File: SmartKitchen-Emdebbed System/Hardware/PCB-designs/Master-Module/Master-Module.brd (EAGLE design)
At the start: 92.3 x 59.7 mm, 24 parts, among them IC2 7805DT, J1 RJ11-2L-B, J2 RJ11-2L-B, J3 RJ11-2L-B, J4 RJ11-2L-B, Q1 BSS123, Q2 BSS123, X1 K375M

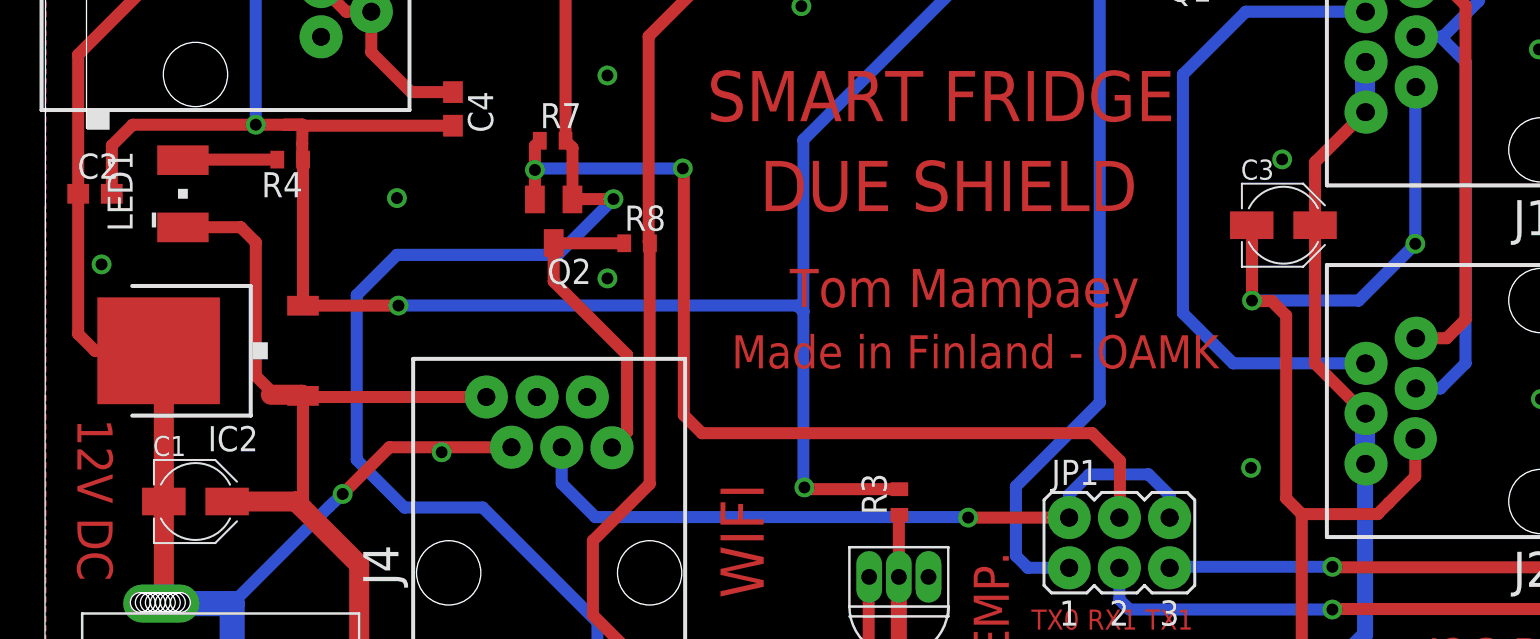
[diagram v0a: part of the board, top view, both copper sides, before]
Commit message: Redesigned wrong component
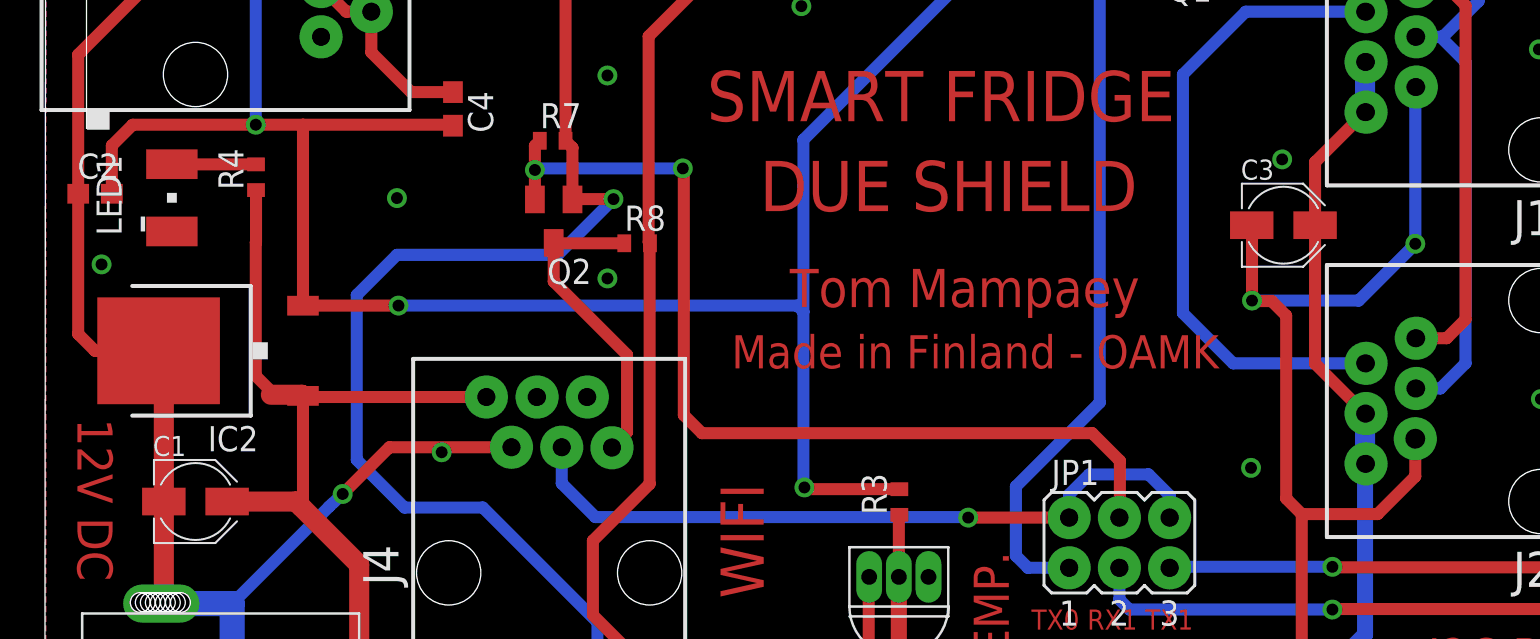
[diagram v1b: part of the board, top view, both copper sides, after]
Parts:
- moved R4 1.94 mm to (10.7, 34.2), turned to 90 degrees
- moved LED1 0.59 mm to (6.43, 33.1)
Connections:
- removed net N$10: C1.+, C3.+, IC2.1, J1.1, J1.3, J2.1, J2.3, J4.1, LED1.C, U$1.VIN, X1.P$7
- new net N$47: C1.+, C3.+, IC2.1, J1.1, J1.3, J2.1, J2.3, J4.1, R4.1, U$1.VIN, X1.P$7
- net AGND: now also LED1.C
- net N$8: no longer R4.1
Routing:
- net N$10: track 135.3 -> 0.00 mm
- net N$47: track 0.00 -> 134.0 mm
- net N$8: track 122.8 -> 121.7 mm
- net N$7: track 4.78 -> 4.26 mm
